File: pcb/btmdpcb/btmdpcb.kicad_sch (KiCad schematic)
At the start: 24 parts, among them Q1 BSD235C, Q3 2N7000, Q4 2N7000, Q5 BSD235C

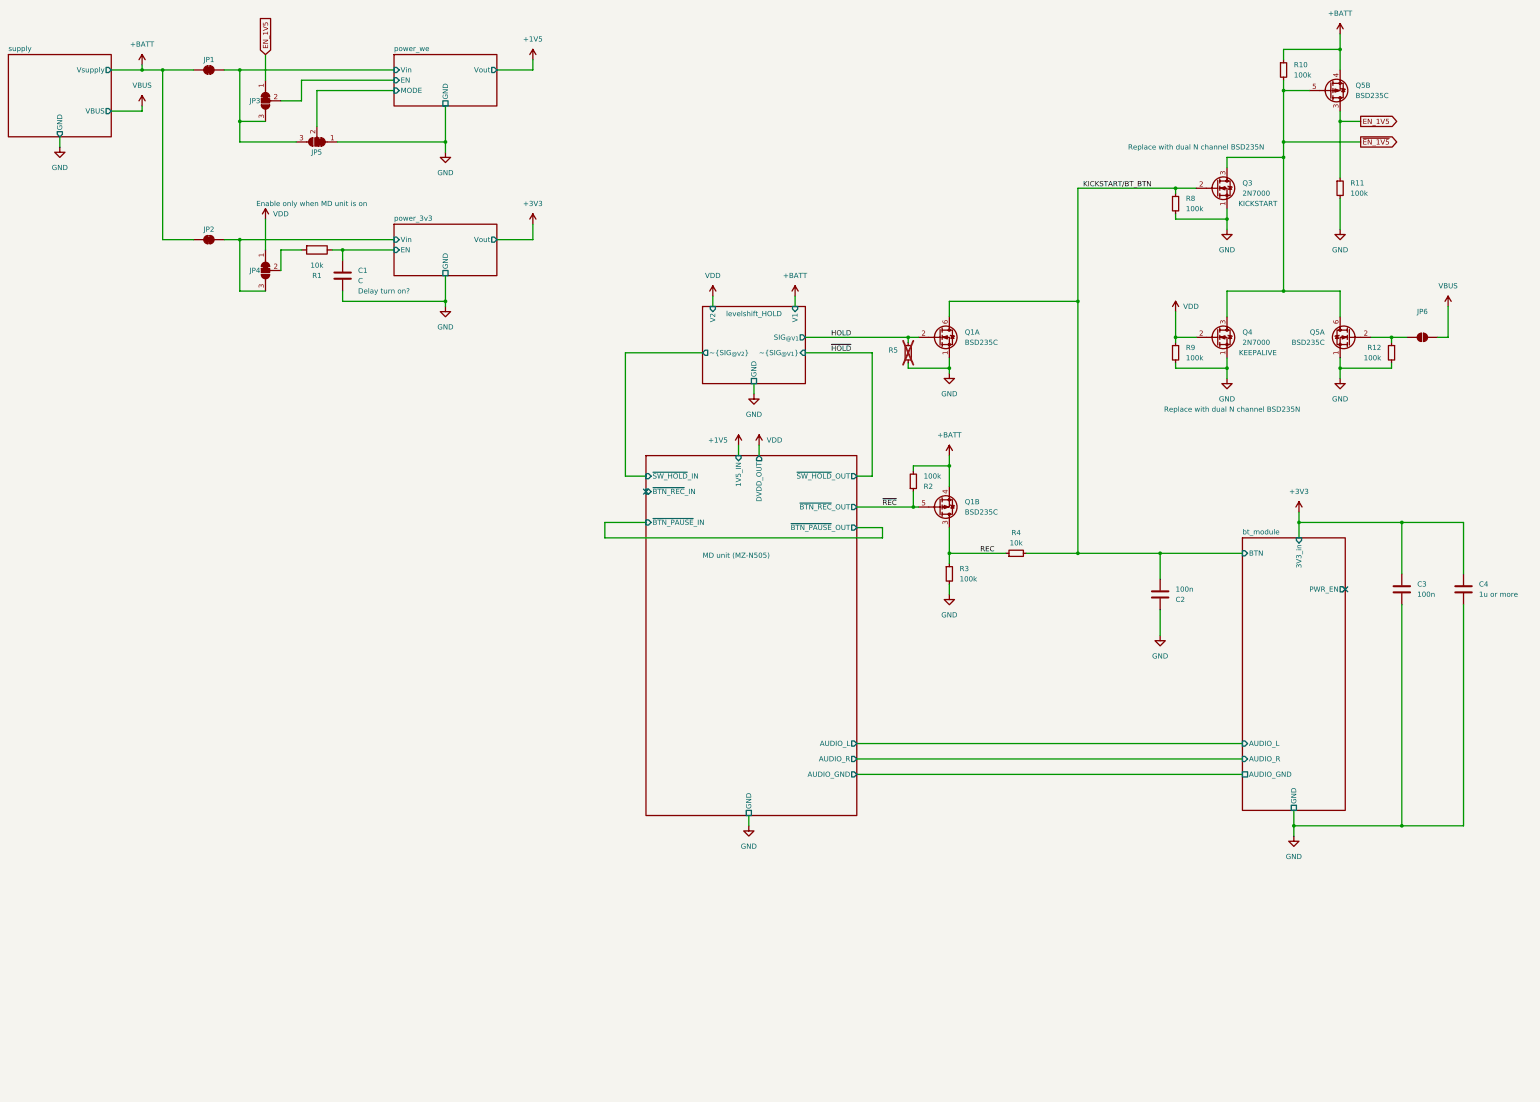
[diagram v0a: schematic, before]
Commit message: Add BT auto-powerup (RC circuit + comparator)
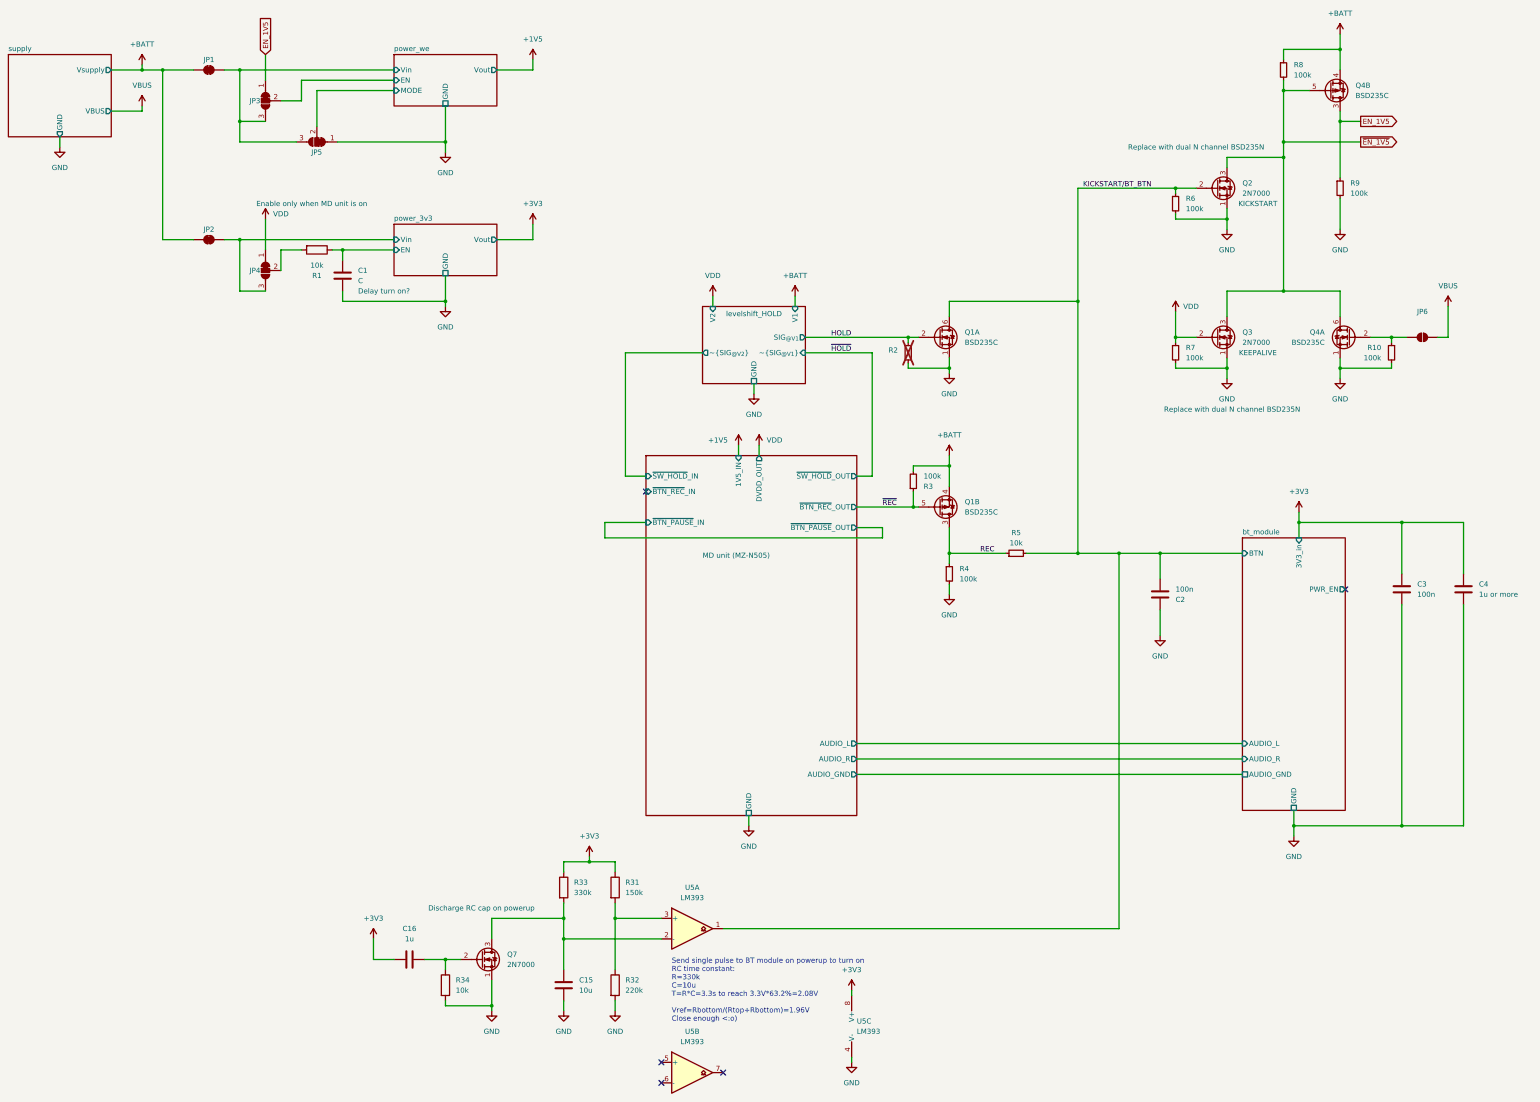
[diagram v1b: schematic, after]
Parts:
- added C15: 10u, symbol Device:C
- added C16: 1u, symbol Device:C
- added Q7: 2N7000, Package_TO_SOT_THT:TO-92_Inline, symbol Transistor_FET:2N7000
- added R31: 150k, symbol Device:R
- added R32: 220k, symbol Device:R
- added R33: 330k, symbol Device:R
- added R34: 10k, symbol Device:R
- added U5: LM393, symbol Comparator:LM393
- renumbered Q3 to Q2, Q4 to Q3, Q5 to Q4, R12 to R10, R5 to R2, R2 to R3, R3 to R4, R4 to R5, R8 to R6, R9 to R7, R10 to R8, R11 to R9
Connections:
- net +3V3: now also C16.1, R31.1, R33.1, U5.8 (V+)
- net GND: now also C15.2, Q7.1 (S), R32.2, R34.2, U5.4 (V-)
- net KICKSTART/BT_BTN: now also U5.1
- new net: C16.2, Q7.2 (G), R34.1
- new net: C15.1, Q7.3 (D), R33.2, U5.2 (-)
- new net: R31.2, R32.1, U5.3 (+)
- no-connect marks 2 -> 5
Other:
- note added: "Send single pulse to BT module on powerup to turn on RC time constant: R=330k C=10u T=R*C=3.3s to reach 3.3V*63.2%=2.08V Vref=Rbottom/(Rtop+Rbottom)=1.96V Close enough <:o)"

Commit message: Create and use BSD235N symbol
to replace 2N7000 N-MOSFETS used temporarily up to now
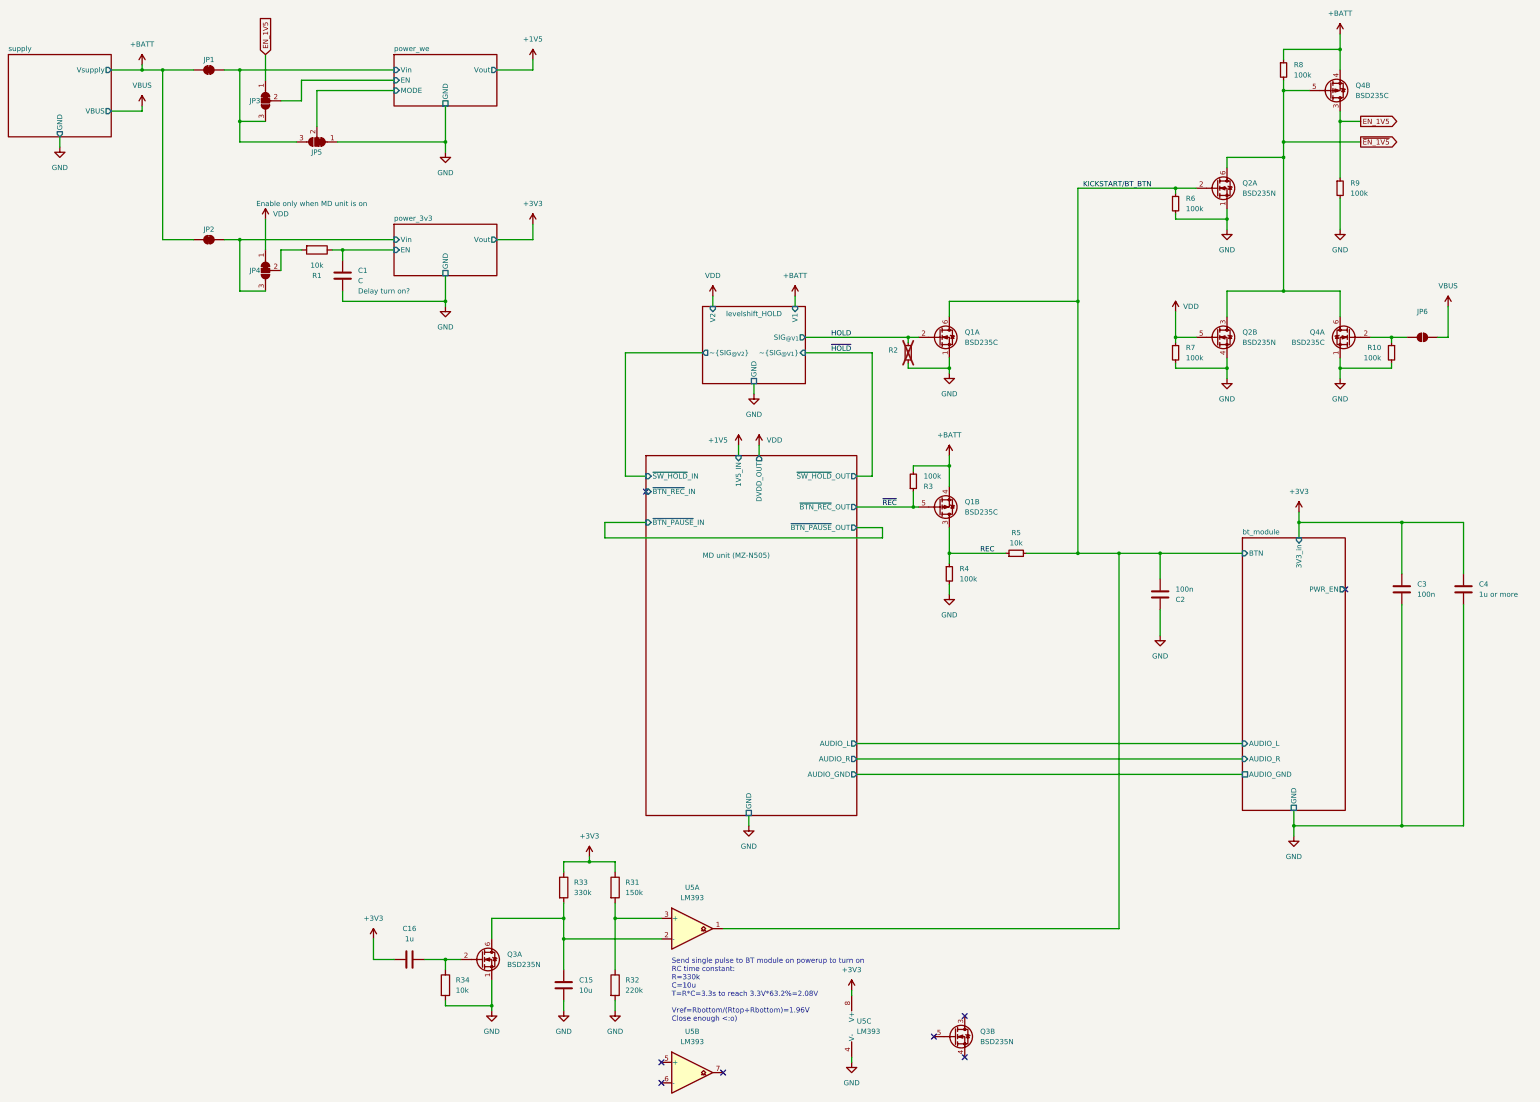
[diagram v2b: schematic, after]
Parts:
- removed Q2, Q3, Q7: 2N7000, Package_TO_SOT_THT:TO-92_Inline, symbol Transistor_FET:2N7000
- added Q2, Q3: BSD235N, Package_TO_SOT_SMD:SOT-363_SC-70-6, symbol mosfet:BSD235N
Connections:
- net GND: now also Q2.1 (S1), Q2.4 (S2), Q3.1 (S1)
- net KICKSTART/BT_BTN: now also Q2.2 (G1)
- net VDD: now also Q2.5 (G2)
- net ~{EN_1V5}: now also Q2.3 (D2), Q2.6 (D1)
- net at C16.2, R34.1: now also Q3.2 (G1)
- net at C15.1, R33.2, U5.2 (-): now also Q3.6 (D1)
- no-connect marks 5 -> 8

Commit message: Add missing libraries, assign all footprints
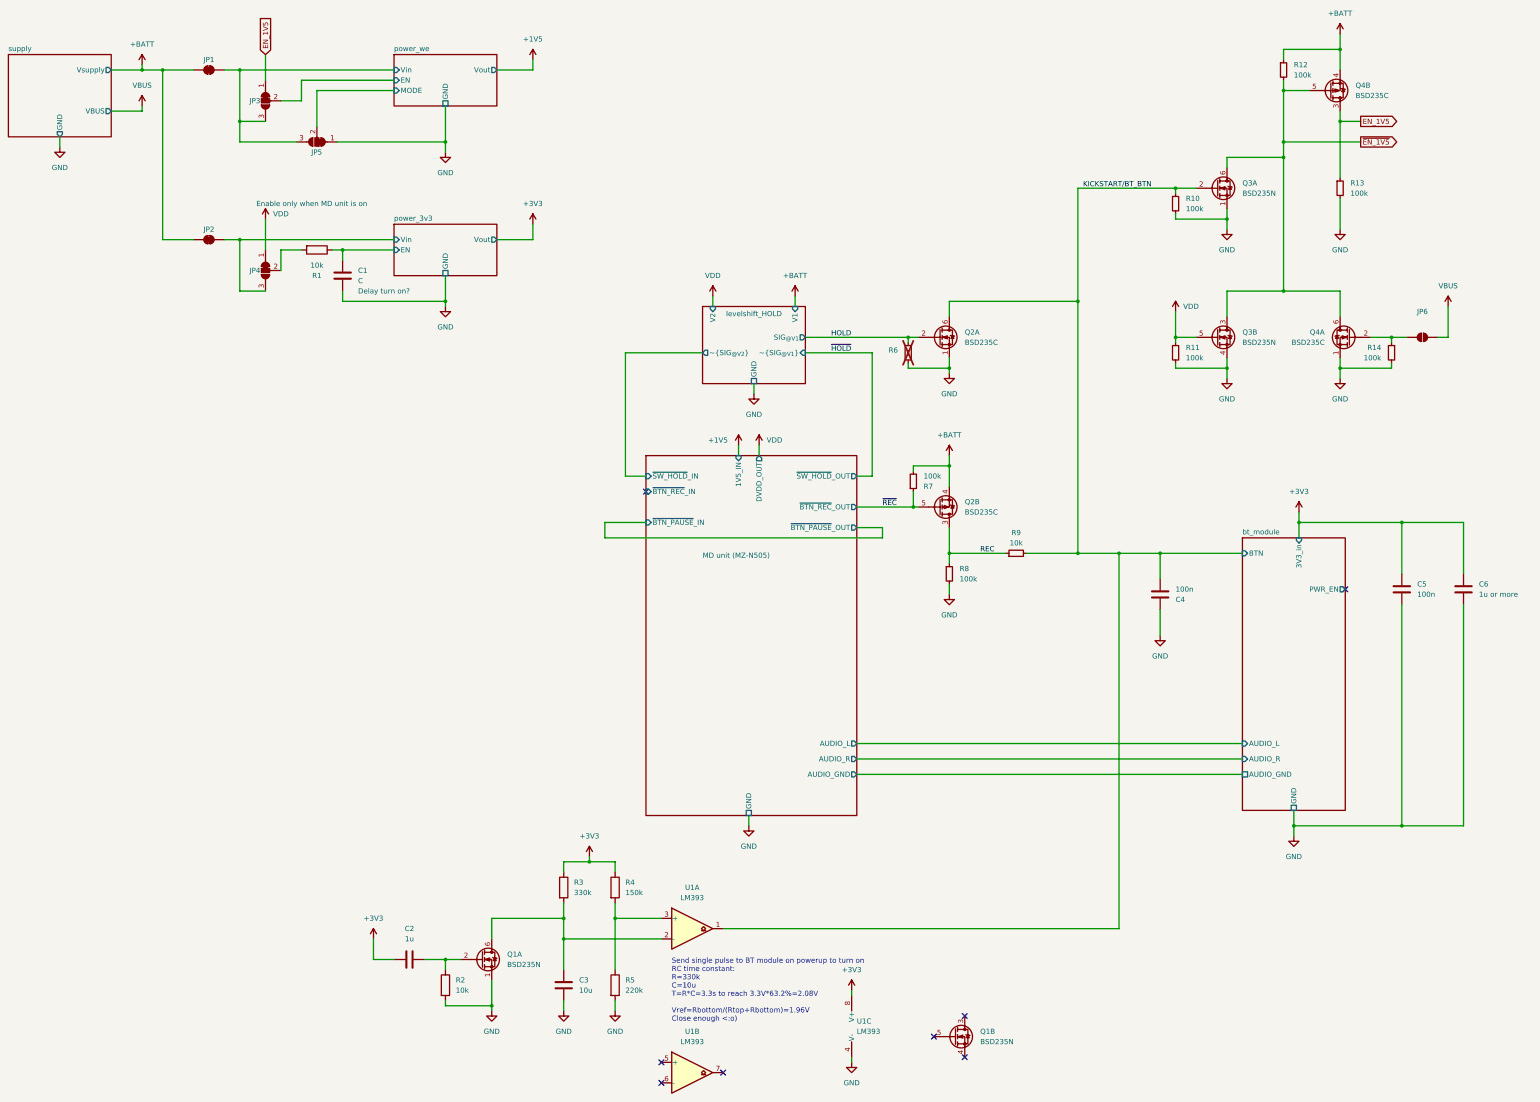
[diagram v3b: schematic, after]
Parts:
- C1: footprint (none) -> Capacitor_SMD:C_0805_2012Metric_Pad1.18x1.45mm_HandSolder
- C2: renamed from C16; footprint (none) -> Capacitor_SMD:C_0805_2012Metric_Pad1.18x1.45mm_HandSolder
- C3: renamed from C15; footprint (none) -> Capacitor_SMD:C_0805_2012Metric_Pad1.18x1.45mm_HandSolder
- C4: renamed from C2; footprint (none) -> Capacitor_SMD:C_0805_2012Metric_Pad1.18x1.45mm_HandSolder
- C5: renamed from C3; footprint (none) -> Capacitor_SMD:C_0805_2012Metric_Pad1.18x1.45mm_HandSolder
- C6: renamed from C4; footprint (none) -> Capacitor_SMD:C_0805_2012Metric_Pad1.18x1.45mm_HandSolder
- JP3, JP4, JP5: footprint (none) -> Jumper:SolderJumper-3_P1.3mm_Bridged12_RoundedPad1.0x1.5mm
- R1: footprint (none) -> Resistor_SMD:R_0805_2012Metric_Pad1.20x1.40mm_HandSolder
- R10: renamed from R6; footprint (none) -> Resistor_SMD:R_0805_2012Metric_Pad1.20x1.40mm_HandSolder
- R11: renamed from R7; footprint (none) -> Resistor_SMD:R_0805_2012Metric_Pad1.20x1.40mm_HandSolder
- R12: renamed from R8; footprint (none) -> Resistor_SMD:R_0805_2012Metric_Pad1.20x1.40mm_HandSolder
- R13: renamed from R9; footprint (none) -> Resistor_SMD:R_0805_2012Metric_Pad1.20x1.40mm_HandSolder
- R14: renamed from R10; footprint (none) -> Resistor_SMD:R_0805_2012Metric_Pad1.20x1.40mm_HandSolder
- R2: renamed from R34; footprint (none) -> Resistor_SMD:R_0805_2012Metric_Pad1.20x1.40mm_HandSolder
- R3: renamed from R33; footprint (none) -> Resistor_SMD:R_0805_2012Metric_Pad1.20x1.40mm_HandSolder
- R4: renamed from R31; footprint (none) -> Resistor_SMD:R_0805_2012Metric_Pad1.20x1.40mm_HandSolder
- R5: renamed from R32; footprint (none) -> Resistor_SMD:R_0805_2012Metric_Pad1.20x1.40mm_HandSolder
- R7: renamed from R3; footprint (none) -> Resistor_SMD:R_0805_2012Metric_Pad1.20x1.40mm_HandSolder
- R8: renamed from R4; footprint (none) -> Resistor_SMD:R_0805_2012Metric_Pad1.20x1.40mm_HandSolder
- R9: renamed from R5; footprint (none) -> Resistor_SMD:R_0805_2012Metric_Pad1.20x1.40mm_HandSolder
- U1: renamed from U5; footprint (none) -> Package_TO_SOT_SMD:SOT-23-8_Handsoldering
- renumbered Q3 to Q1, Q1 to Q2, Q2 to Q3, R2 to R6

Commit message: Correct footprints, fix issues on update PCB from schematic
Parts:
- Q1, Q2, Q3, Q4: footprint Package_TO_SOT_SMD:SOT-363_SC-70-6 -> Package_TO_SOT_SMD:SOT-363_SC-70-6_Handsoldering
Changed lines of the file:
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@@
 			)
 		)
-		(property "Footprint" "Package_TO_SOT_SMD:SOT-363_SC-70-6"
+		(property "Footprint" "Package_TO_SOT_SMD:SOT-363_SC-70-6_Handsoldering"
 			(at 147.32 250.825 0)
 			(effects
@@
 			)
 		)
-		(property "Footprint" "Package_TO_SOT_SMD:SOT-363_SC-70-6"
+		(property "Footprint" "Package_TO_SOT_SMD:SOT-363_SC-70-6_Handsoldering"
 			(at 264.16 269.875 0)
 			(effects
@@
 			)
 		)
-		(property "Footprint" "Package_TO_SOT_SMD:SOT-363_SC-70-6"
+		(property "Footprint" "Package_TO_SOT_SMD:SOT-363_SC-70-6_Handsoldering"
 			(at 328.93 60.325 0)
 			(effects
@@
 			)
 		)
-		(property "Footprint" "Package_TO_SOT_SMD:SOT-363_SC-70-6"
+		(property "Footprint" "Package_TO_SOT_SMD:SOT-363_SC-70-6_Handsoldering"
 			(at 356.87 36.195 0)
 			(effects
@@
 			)
 		)
-		(property "Footprint" "Package_TO_SOT_SMD:SOT-363_SC-70-6"
+		(property "Footprint" "Package_TO_SOT_SMD:SOT-363_SC-70-6_Handsoldering"
 			(at 260.35 97.155 0)
 			(effects
@@
 			)
 		)
-		(property "Footprint" "Package_TO_SOT_SMD:SOT-363_SC-70-6"
+		(property "Footprint" "Package_TO_SOT_SMD:SOT-363_SC-70-6_Handsoldering"
 			(at 351.79 97.155 0)
 			(effects
@@
 			)
 		)
-		(property "Footprint" "Package_TO_SOT_SMD:SOT-363_SC-70-6"
+		(property "Footprint" "Package_TO_SOT_SMD:SOT-363_SC-70-6_Handsoldering"
 			(at 260.35 139.065 0)
 			(effects
@@
 			)
 		)
-		(property "Footprint" "Package_TO_SOT_SMD:SOT-363_SC-70-6"
+		(property "Footprint" "Package_TO_SOT_SMD:SOT-363_SC-70-6_Handsoldering"
 			(at 328.93 97.155 0)
 			(effects
@@
 			(project "btmdpcb"
 				(path "/6e43e92f-e106-411c-86ee-217d084aee5b"
-					(page "8")
+					(page "7")
 				)
 			)
@@
 			(project "btmdpcb"
 				(path "/6e43e92f-e106-411c-86ee-217d084aee5b"
-					(page "5")
+					(page "2")
 				)
 			)
@@
 			(project "btmdpcb"
 				(path "/6e43e92f-e106-411c-86ee-217d084aee5b"
-					(page "5")
+					(page "4")
 				)
 			)
@@
 			(project "btmdpcb"
 				(path "/6e43e92f-e106-411c-86ee-217d084aee5b"
-					(page "7")
+					(page "5")
 				)
 			)
@@
 			(project "btmdpcb"
 				(path "/6e43e92f-e106-411c-86ee-217d084aee5b"
-					(page "4")
+					(page "3")
 				)
 			)

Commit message: Layout PCB
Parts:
- removed C1: C, Capacitor_SMD:C_0805_2012Metric_Pad1.18x1.45mm_HandSolder, symbol Device:C
- removed C4, C5: 100n, Capacitor_SMD:C_0805_2012Metric_Pad1.18x1.45mm_HandSolder, symbol Device:C
- removed C6: 1u or more, Capacitor_SMD:C_0805_2012Metric_Pad1.18x1.45mm_HandSolder, symbol Device:C
- JP1: value SolderJumper_2_Bridged -> 1V5_IN
- JP2: value SolderJumper_2_Bridged -> 3V3_IN
- JP3: value SolderJumper_3_Bridged12 -> 1V5_EN
- JP4: value SolderJumper_3_Bridged12 -> 3V3_EN
- JP5: value SolderJumper_3_Bridged12 -> 3V3_MODE
- JP6: value SolderJumper_2_Open -> VBUS_EN
- renumbered C2 to C1, C3 to C2
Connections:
- net +3V3: no longer R3.1, R4.1
- net +BATT renamed +SUPPLY
- net +SUPPLY: now also R3.1, R4.1
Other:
- sheet MD unit (MZ-N505) ports: added none; removed ~{BTN_PAUSE}_IN, ~{BTN_PAUSE}_OUT
